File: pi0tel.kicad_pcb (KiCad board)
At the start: 2 copper layers, 65 x 30 mm, 14 parts, among them J1 DIN-5_180degree, J2 RPi_GPIO, Q1 BSS138, U1 LM2596S-5

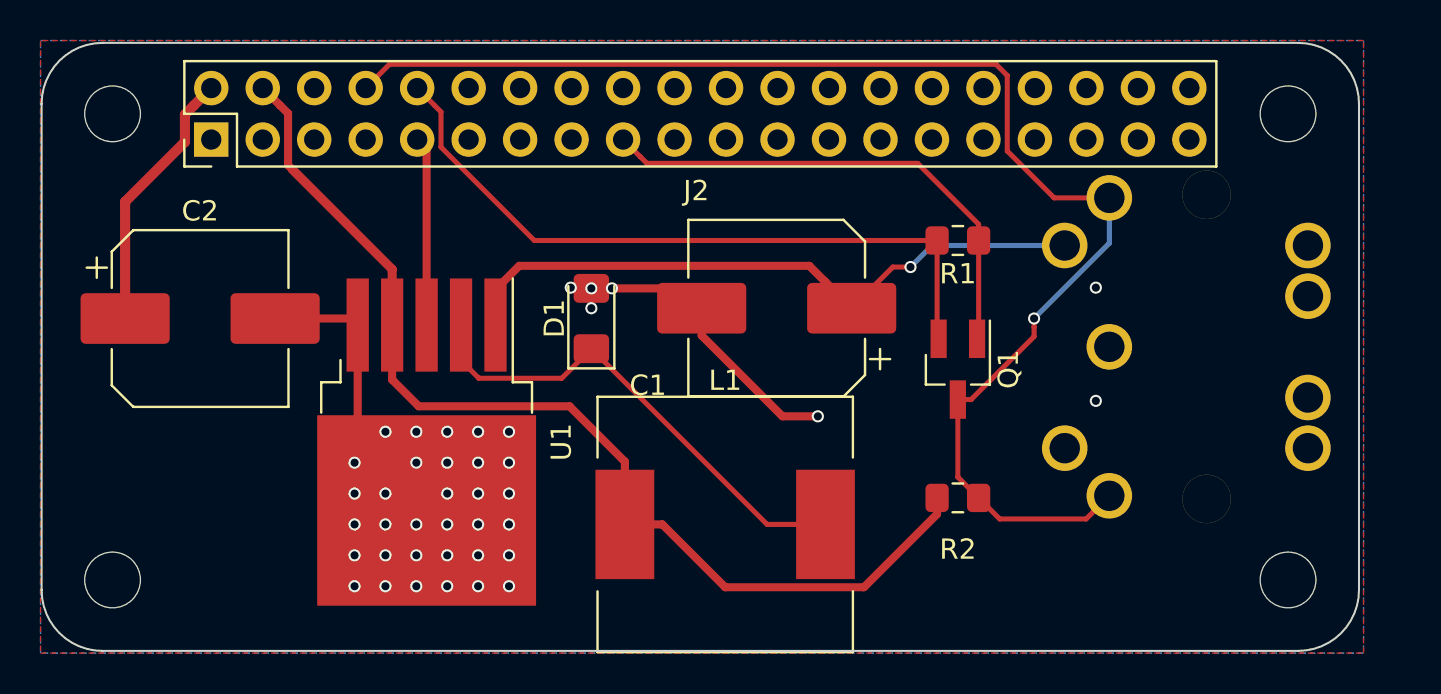
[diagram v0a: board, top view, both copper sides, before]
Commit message: Put din connector on top side.
Also a few adjustments
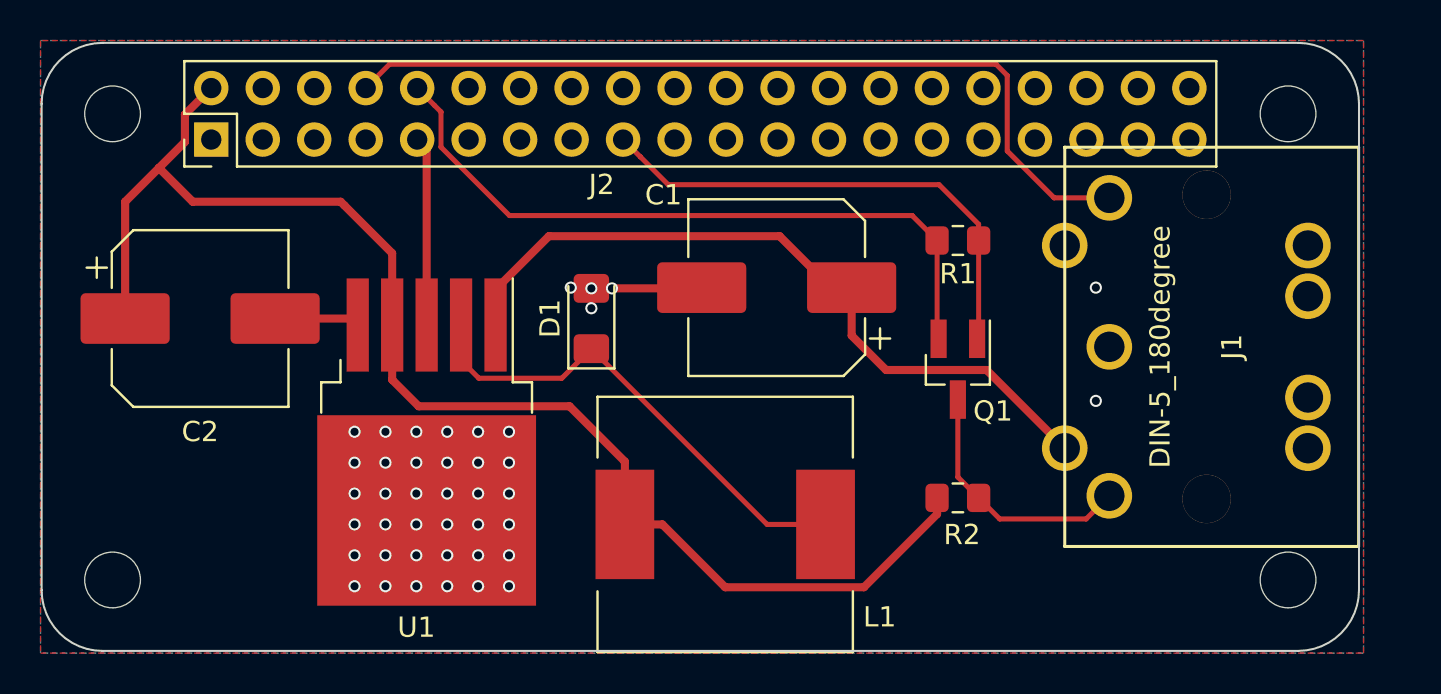
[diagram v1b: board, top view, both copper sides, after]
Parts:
- J1: moved to F.Cu
- moved C1 1.02 mm to (48.8, 36.6)
- turned J1 to 270 degrees
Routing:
- net GND: track 38.7 -> 25.2 mm, vias 40 -> 42
- net /MinitelTx: track 26.1 -> 12.6 mm, vias 1 -> 0
- net /MinitelVcc: track 32.5 -> 36.1 mm, vias 1 -> 0
- net +5V: track 65.4 -> 67.9 mm

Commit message: Increase board size to accomodate for DIN
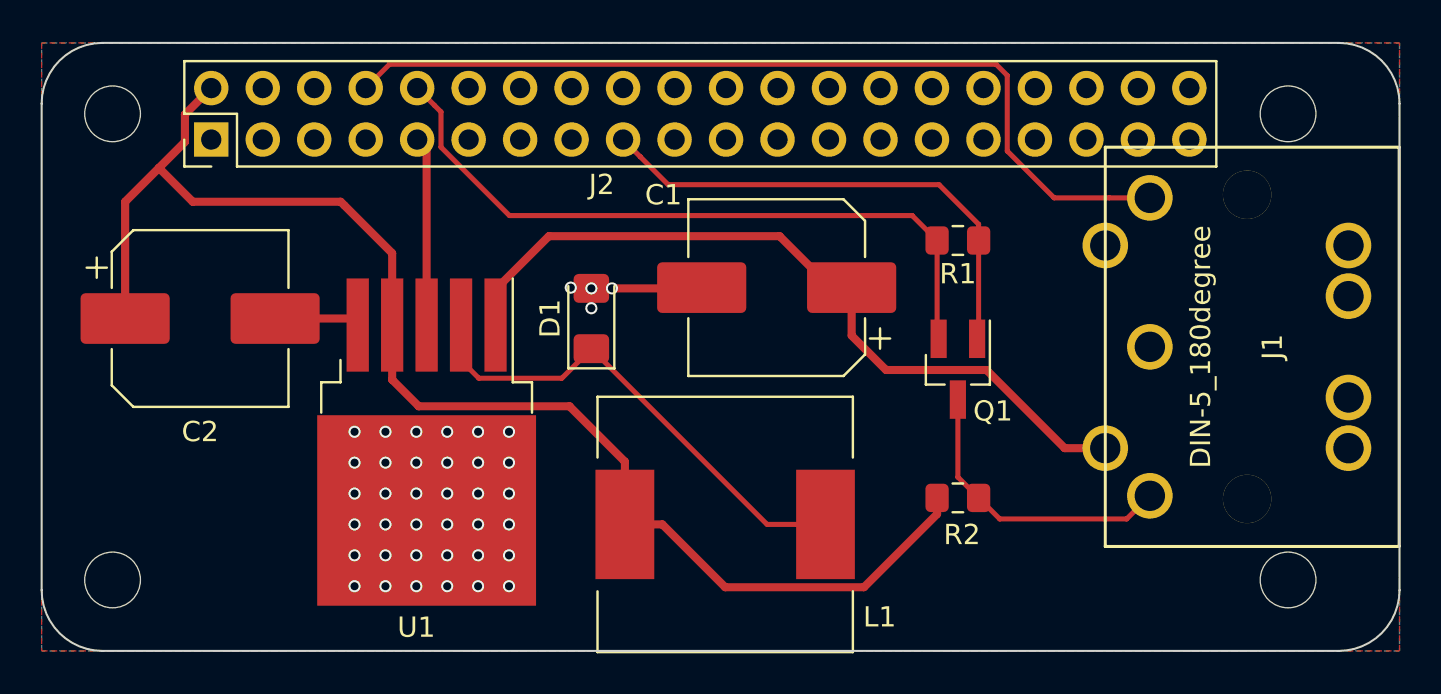
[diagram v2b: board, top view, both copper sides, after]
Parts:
- moved J1 2.00 mm to (72.2, 39.5)
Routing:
- net /MinitelTx: track 12.6 -> 14.6 mm
- net /MinitelRx: track 42.1 -> 44.1 mm
- net /MinitelVcc: track 36.1 -> 38.1 mm
- net GND: vias 42 -> 40
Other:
- board size 65 x 30 mm -> 67 x 30 mm

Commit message: Add some text
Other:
- board text added: "2021"
- board text added: "faxmodem"
- board text added: "pi0tel"
- board text added: "r1"
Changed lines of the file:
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@@
   (general
     (thickness 1.6)
-    (drawings 16)
+    (drawings 20)
     (tracks 115)
     (zones 0)
@@
     )
   )
+  (gr_text r1 (at 67.6 51.9) (layer F.SilkS)
+    (effects (font (size 1.5 1.5) (thickness 0.3)))
+  )
+  (gr_text 2021 (at 50.4 42.8) (layer B.SilkS)
+    (effects (font (size 1.5 1.5) (thickness 0.3)) (justify mirror))
+  )
+  (gr_text faxmodem (at 53.2 40.2) (layer B.SilkS)
+    (effects (font (size 1.5 1.5) (thickness 0.3)) (justify mirror))
+  )
+  (gr_text pi0tel (at 60.7 51.8) (layer F.SilkS)
+    (effects (font (size 1.5 1.5) (thickness 0.3)))
+  )
   (gr_arc (start 15.5 27.5) (end 12.5 27.5) (angle 90) (layer Edge.Cuts) (width 0.1))

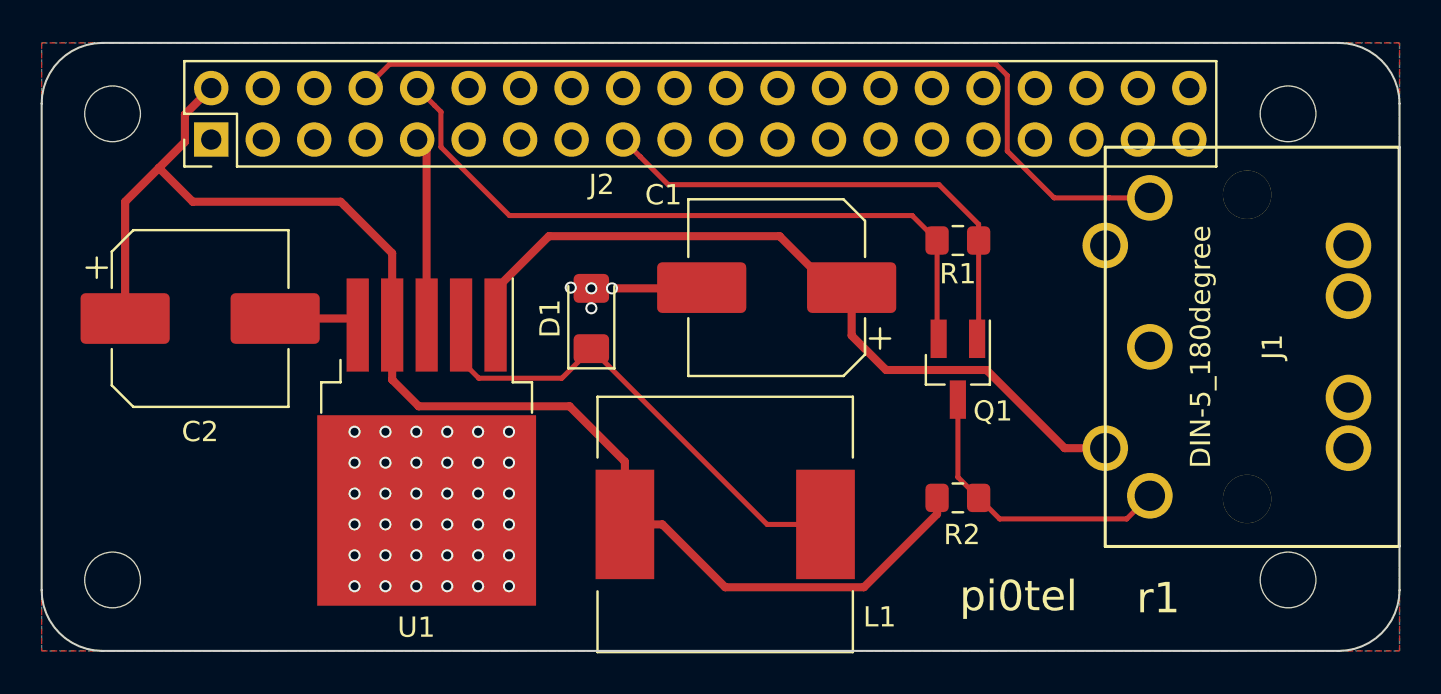
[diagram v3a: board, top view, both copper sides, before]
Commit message: Fix footprint for Schottky
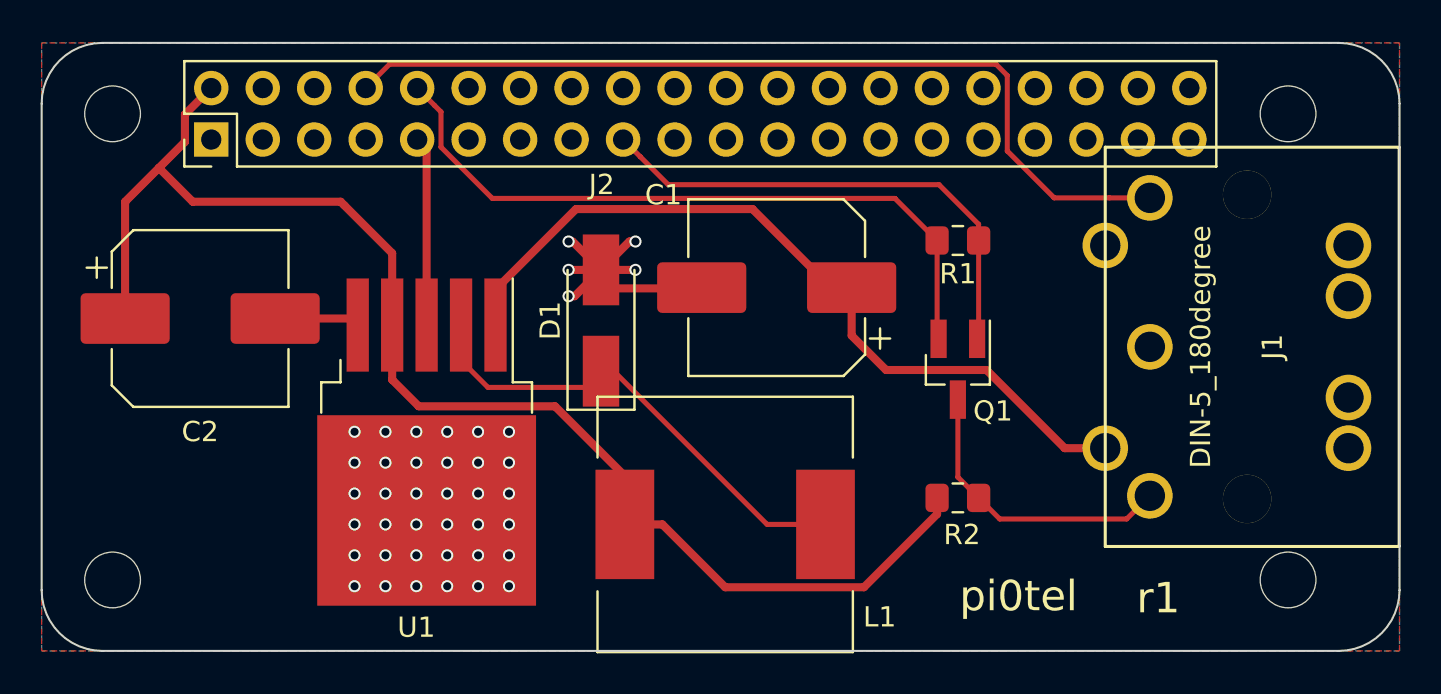
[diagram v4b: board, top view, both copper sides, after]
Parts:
- D1: footprint Diode_SMD:D_1206_3216Metric_Pad1.42x1.75mm_HandSolder -> Diode_SMD:D_SMA_Handsoldering
- moved D1 0.49 mm to (40.1, 38.2)
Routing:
- net GND: track 25.2 -> 35.1 mm, vias 40 -> 41
- net /MinitelVcc: track 38.1 -> 39.2 mm

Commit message: Enlarge inductance pads for handsolder
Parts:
- L1: footprint Inductor_SMD:L_12x12mm_H6mm -> custom:L_12x12mm_H6mm_handsolder
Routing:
- net +5V: track 67.4 -> 69.5 mm
